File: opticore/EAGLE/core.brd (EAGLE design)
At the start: 100.3 x 82.6 mm, 121 parts, among them IC1 MCP1825S-3302E, IC2 MC33269T-5.0, J1 POWER_JACKSLT, Q1 MMDT3904, Q2 2N3904, Q3 2N3904, Q4 2N3904, Q5 2N3904, Q6 2N3904, Q7 2N3904, Q8 2N3904, U2 STM32F10XCXT6, U3 SST25VF040B-S2, U4 NL17SZ125SOT553, X1 USB-MICROB, X2 IPEX-20279-001E, Y1 32Khz, Y2 8Mhz

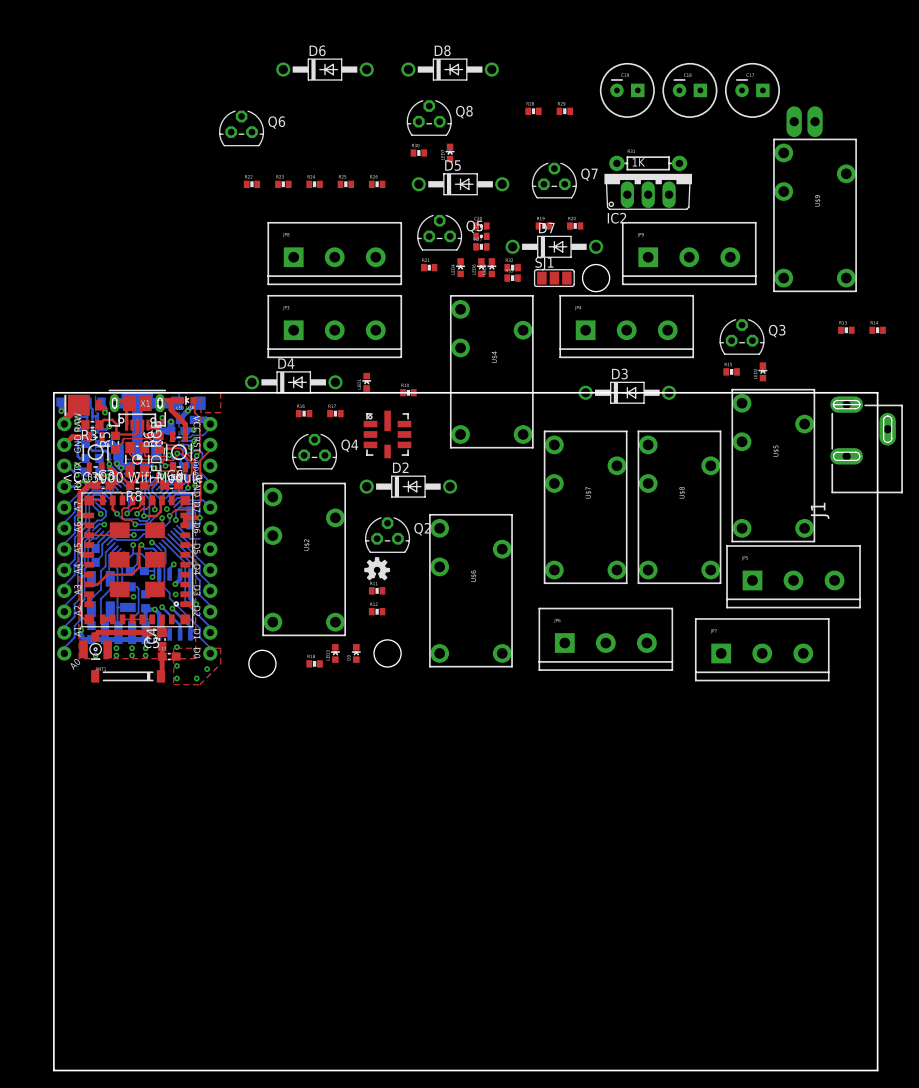
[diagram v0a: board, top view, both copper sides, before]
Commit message: Initial placement of relays
Still need to do a lot of work. Placement is temporary.

LEDs and the rest of the components need to be placed.

One problem is that I can't move what they originally did. Option #1: Redo what they did. (not happening) Option #2: Try adding their schematic as a part then placing it on a new shm. Option #3: Try to find a way to move it online.

Signed-off-by: Scott Lerner <scottphiliplerner@gmail.com>
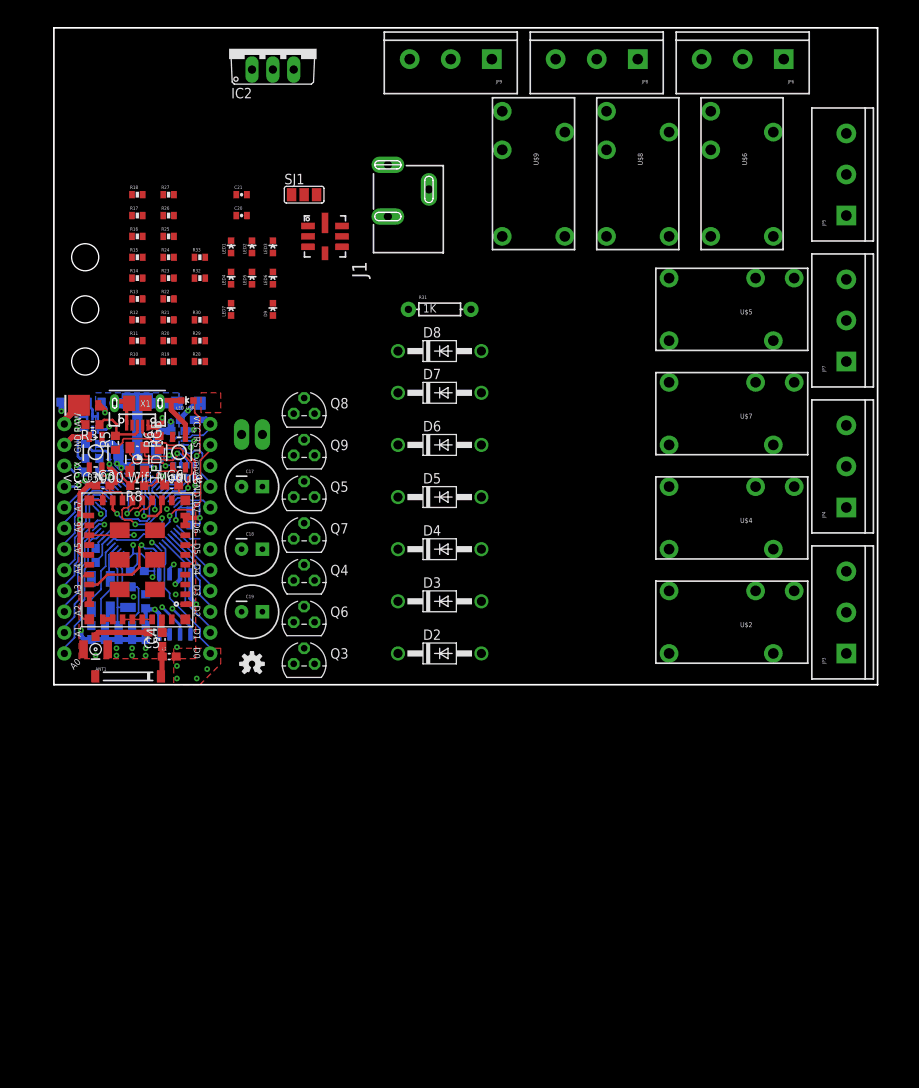
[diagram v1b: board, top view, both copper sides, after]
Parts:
- removed Q1: MMDT3904, SparkFun-DiscreteSemi:SOT363
- removed U$1: SPARK_LOGO2, Spark:SPARK_LOGO2
- added Q9: 2N3904, transistor-npn:TO92
- Q2: value 2N3904 -> MMDT3904; device transistor-npn:TO92 -> SparkFun-DiscreteSemi:SOT363
- moved R14 90.4 mm to (10.2, 49.5)
- moved R13 86.4 mm to (10.2, 47.0)
- moved C19 78.2 mm to (24.1, 8.89)
- moved JP3 78.0 mm to (96.5, 3.81), turned to 90 degrees
- moved C17 77.8 mm to (24.1, 24.1)
- moved JP10 77.3 mm to (22.9, 30.5)
- moved C18 77.3 mm to (24.1, 16.5)
- moved JP6 76.0 mm to (88.9, 76.2), turned to 180 degrees
- moved R15 73.7 mm to (10.2, 52.1)
- moved Q3 66.3 mm to (30.5, 2.54)
- moved LED2 64.1 mm to (24.1, 53.3)
- moved J1 63.1 mm to (38.1, 49.5)
- moved STANDOFF2 62.3 mm to (3.81, 52.1)
- moved R18 61.1 mm to (10.2, 59.7)
- moved U$6 60.6 mm to (83.8, 63.5)
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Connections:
- net +3V3: now also Q2.3; no longer Q1.3
- net GND: now also Q2.1, Q9.3; no longer Q1.1, Q2.3
- net N$13: now also Q2.5, Q2.6; no longer Q1.5, Q1.6
- net N$16: now also Q2.4; no longer Q1.4
- net N$18: now also Q3.1; no longer Q2.1
- net N$19: now also Q4.1; no longer Q3.1
- net N$20: now also Q4.2; no longer Q3.2
- net N$22: now also Q6.1; no longer Q4.1
- net N$23: now also Q6.2; no longer Q4.2
- net N$24: now also Q3.2; no longer Q2.2
- net N$26: now also Q7.1; no longer Q5.1
- net N$27: now also Q7.2; no longer Q5.2
- net N$29: now also Q5.1; no longer Q6.1
- net N$30: now also Q5.2; no longer Q6.2
- net N$32: now also Q8.1; no longer Q7.1
- net N$33: now also Q8.2; no longer Q7.2
- net N$35: now also Q9.1; no longer Q8.1
- net N$36: now also Q9.2; no longer Q8.2
- net N$8: now also Q2.2; no longer Q1.2
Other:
- board size 100.3 x 82.6 mm -> 100.3 x 80 mm

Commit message: Finished Initial Placement
I still need to route everything, but I think it's a pretty
space-efficient design as is. Probably needs to be organized a little
better.

NOTE: With the free version of EAGLE, I cannot make a board bigger than
100mm x 80mm. In those dimensions, I cannot place all relays in a
straight line. Hence the inverted 'L' shape.
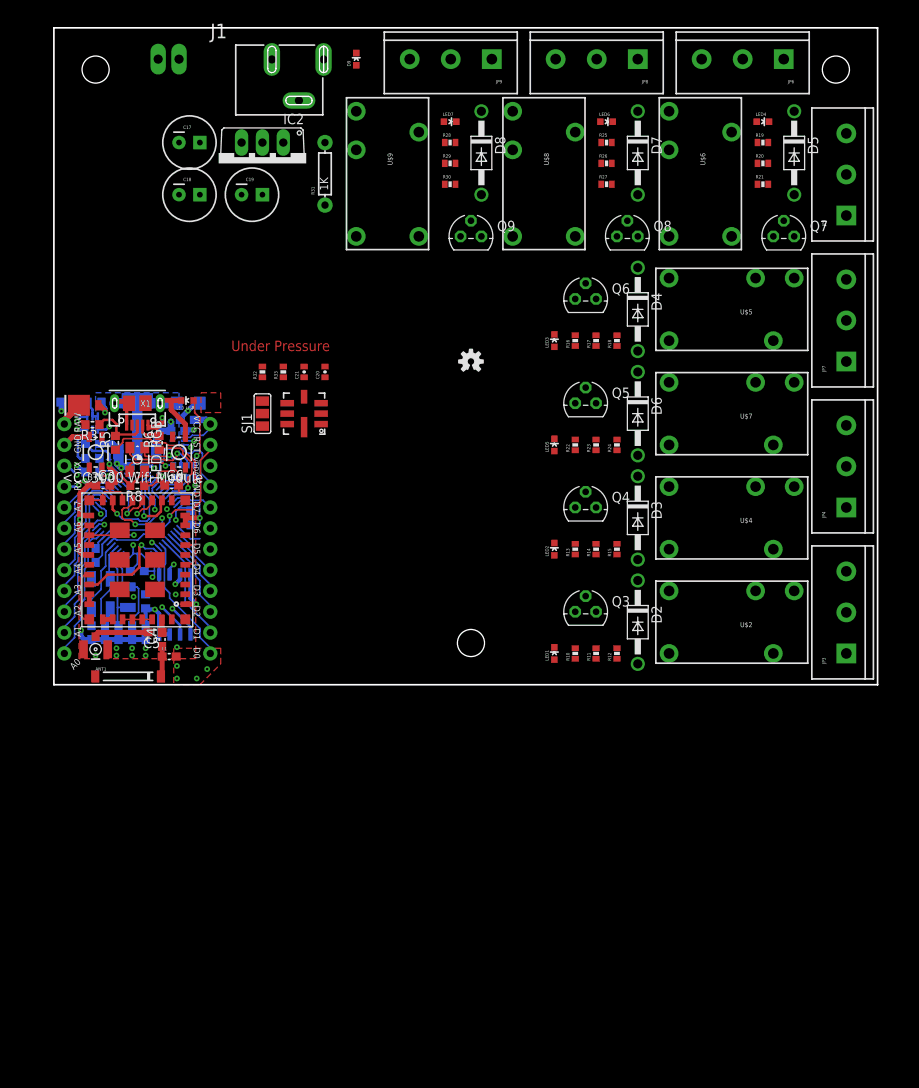
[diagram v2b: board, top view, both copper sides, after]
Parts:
- moved STANDOFF2 94.3 mm to (95.2, 74.9)
- moved R19 77.1 mm to (86.4, 66.0)
- moved R20 75.5 mm to (86.4, 63.5)
- moved R21 74.2 mm to (86.4, 61.0)
- moved R12 71.2 mm to (68.6, 3.81), turned to 90 degrees
- moved Q7 69.1 mm to (88.9, 54.6)
- moved R15 68.4 mm to (68.6, 16.5), turned to 90 degrees
- moved R11 67.6 mm to (66.0, 3.81), turned to 90 degrees
- moved LED4 67.5 mm to (86.4, 68.6), turned to 270 degrees
- moved R14 64.9 mm to (66.0, 16.5), turned to 90 degrees
- moved R10 64.1 mm to (63.5, 3.81), turned to 90 degrees
- moved LED1 63.3 mm to (61.0, 3.81)
- moved R13 61.4 mm to (63.5, 16.5), turned to 90 degrees
- moved R18 61.1 mm to (68.6, 41.9), turned to 90 degrees
- moved D5 60.2 mm to (90.2, 64.8), turned to 270 degrees
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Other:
- board text added: "Under Pressure"

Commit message: Close to final revision
I'm working on laying down the final placement as well as the ground
planes. I'll try and work on it soon.
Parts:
- removed ANT1: AT8010, Spark:AT8010
- removed BTN, RESET: KMR211GLFS, Spark:TACTILE_SWITCH_SMD
- removed C1, C2: 4.7uF, rcl:C0603
- removed C10, C11: 22pF, rcl:C0603
- removed C12, C13, C14, C16, C3, C6, C7: 100nF, rcl:C0603
- removed C15: 10uF, Spark:EIA3216
- removed C4: 2.2pF, rcl:C0603
- removed C5, C8, C9: 10pF, rcl:C0603
- removed D8: 1N4004, diode:DO41-10
- removed D9: GREEN, SparkFun-LED:LED-0603
- removed IC1: MCP1825S-3302E, Spark:SOT223
- removed JP1, JP2: M12PTH, Spark:1X12-SMALL-PADS
- removed JP3, JP4, JP5, JP6, JP7, JP8, JP9: (no value), SparkFun-Connectors:SCREWTERMINAL-5MM-3
- removed L1: 2.2nH, SparkFun-Passives:0603
- removed L2: Bead, SparkFun-Passives:0603
- removed LED_RGB: (no value), Spark:P-LCC-4-3
- removed LED_USR: (no value), SparkFun:LED-0603
- removed LOGO1: OSHW-LOGOS, SparkFun-Aesthetics:OSHW-LOGO-S
- removed Q8, Q9: 2N3904, transistor-npn:TO92
- removed R25, R27, R28, R30: 1K, SparkFun-Passives:0402-RES
- removed R26, R29: 10K, SparkFun-Passives:0402-RES
- removed R31: 1K, SparkFun-Passives:AXIAL-0.3
- removed R32, R33: 4.7K, SparkFun-Passives:0402-RES
- removed RN1: EXB-38V102JV, resistor-dil:EXB38V
- removed STANDOFF1, STANDOFF2, STANDOFF3: STAND-OFF, SparkFun-Electromechanical:STAND-OFF
- removed U1: (no value), CC3000:CC3000
- removed U2: STM32F10XCXT6, stm32:TQFP48
- removed U3: SST25VF040B-S2, Spark:SOIC127P790X216-8N
- removed U4: NL17SZ125SOT553, Spark:SOT-553
- removed X2: IPEX-20279-001E, Spark:IPEX-20279-001E
- removed Y1: 32Khz, Spark:FC135
- removed Y2: 8Mhz, SparkFun-FreqCtrl:CRYSTAL-SMD-5X3
- added JP11, JP12: M12PTH, Spark:1X12-SMALL-PADS
- added LED8: (no value), SparkFun-LED:LED3MM
- added LOGO2: OSHW-LOGOL, SparkFun-Aesthetics:OSHW-LOGO-L
- added Q1: 2N3904, transistor-npn:TO92
- C17, C18, C19: value (none) -> 100uF
- D1: value DIODE -> 1N4004; device Spark:DIODE-DO-220AA(SMP) -> diode:DO41-10
- LED1, LED2, LED3, LED4, LED5, LED6, LED7: value RED -> (none); device SparkFun-LED:LED-0603 -> SparkFun-LED:LED3MM
- Q2: value MMDT3904 -> 2N3904; device SparkFun-DiscreteSemi:SOT363 -> transistor-npn:TO92
- R1, R8: value 10K -> 1K; device rcl:R0603 -> SparkFun-Resistors:AXIAL-0.3
- R10, R13, R16, R19, R24: device SparkFun-Passives:0402-RES -> SparkFun-Resistors:AXIAL-0.3
- R11, R14, R17, R20: value 10K -> 1K; device SparkFun-Passives:0402-RES -> SparkFun-Resistors:AXIAL-0.3
- R12, R15, R18, R21: value 1K -> 10K; device SparkFun-Passives:0402-RES -> SparkFun-Resistors:AXIAL-0.3
- R2: value 33K -> 1K; device rcl:R0603 -> SparkFun-Resistors:AXIAL-0.3
- R22: value 1K -> 4.7K; device SparkFun-Passives:0402-RES -> SparkFun-Resistors:AXIAL-0.3
- R23: value 10K -> 4.7K; device SparkFun-Passives:0402-RES -> SparkFun-Resistors:AXIAL-0.3
- R3: value 1K5 -> 10K; device rcl:R0603 -> SparkFun-Resistors:AXIAL-0.3
- R4: device rcl:R0603 -> SparkFun-Resistors:AXIAL-0.3
- R5: value 22 -> 1K; device rcl:R0603 -> SparkFun-Resistors:AXIAL-0.3
- R6: value 22 -> 10K; device rcl:R0603 -> SparkFun-Resistors:AXIAL-0.3
- R7: value 47K -> 1K; device rcl:R0603 -> SparkFun-Resistors:AXIAL-0.3
- R9: value 1K -> 10K; device rcl:R0603 -> SparkFun-Resistors:AXIAL-0.3
- X1: value USB-MICROB -> FFKV8; device Spark:USB-MICROB-SLOT-HOLE -> con-phoenix-508:FFKV8
- moved JP10 106.0 mm to (88.9, 2.54), turned to 180 degrees
- moved J1 99.0 mm to (73.7, -3.81), turned to 0 degrees
- moved C17 89.5 mm to (86.4, 10.2), turned to 270 degrees
- moved SJ1 72.7 mm to (91.4, 63.5), turned to 0 degrees
- moved C19 72.2 mm to (69.8, 3.81), turned to 270 degrees
- moved C18 70.9 mm to (67.3, 10.2), turned to 270 degrees
- moved IC2 70.6 mm to (61.0, 2.54)
- moved U$2 67.5 mm to (17.8, 21.6), turned to 180 degrees
- moved C20 65.1 mm to (94.0, 61.0)
- moved U$3 65.1 mm to (91.4, 55.9)
- moved C21 62.7 mm to (88.9, 61.0)
- moved LED1 58.4 mm to (20.3, 45.7), turned to 90 degrees
- moved U$8 54.2 mm to (94.0, 21.6), turned to 180 degrees
- moved LED7 53.4 mm to (96.5, 45.7), turned to 90 degrees
- moved U$4 53.4 mm to (30.5, 21.6), turned to 180 degrees
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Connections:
- removed net BTN: BTN.3, U2.20
- removed net LED1: LED_USR.A, RN1.4
- removed net LED2: RN1.8, U2.29
- removed net LED3: RN1.7, U2.30
- removed net LED4: RN1.6, U2.31
- removed net MAIN1: JP3.2, U$2.4
- removed net MAIN2: JP4.2, U$4.4
- removed net MAIN3: JP7.2, U$7.4
- removed net MAIN4: JP5.2, U$5.4
- removed net MAIN5: JP6.2, U$6.4
- removed net MAIN6: JP8.2, U$8.4
- removed net MAIN7: JP9.2, U$9.4
- removed net MEM_CS: R9.1, U2.46, U3.1
- removed net N$10: LED_RGB.1, RN1.1
- removed net N$12: LED_RGB.3, RN1.2
- removed net N$13: Q2.5, Q2.6, R1.1, R2.2
- removed net N$14: LED_RGB.4, RN1.3
- removed net N$15: U1.SDA_CC3000, U1.SDA_EEPROM
- removed net N$16: Q2.4, R3.2
- removed net N$17: LED2.A, R13.1
- removed net N$21: LED3.A, R16.1
- removed net N$25: LED4.A, R19.1
- removed net N$28: LED5.A, R22.1
- removed net N$31: LED6.A, R25.1
- removed net N$34: LED7.A, R28.1
- removed net N$43: R32.2, SJ1.3
- removed net N$44: R33.2, SJ1.1
- removed net NC1: JP3.3, U$2.2
- removed net NC2: JP4.3, U$4.2
- removed net NC3: JP7.3, U$7.2
- removed net NC4: JP5.3, U$5.2
- removed net NC5: JP6.3, U$6.2
- removed net NC6: JP8.3, U$8.2
- removed net NC7: JP9.3, U$9.2
- removed net OSC32_IN: C9.1, U2.3, Y1.X1
- removed net OSC32_OUT: C8.1, U2.4, Y1.X2
- removed net OSC_IN: C11.1, U2.5, Y2.1
- removed net OSC_OUT: C10.1, U2.6, Y2.3
- removed net SPI_DOUT: U1.SPI_DOUT, U4.IN
- removed net SPI_MISO: U2.27, U3.2, U4.OUT
- removed net SPI_MOSI: U1.SPI_DIN, U2.28, U3.5
- removed net SPI_SCK: U1.SPI_CLK, U2.26, U3.6
- removed net USBM: R6.1, U2.32
- removed net USBP: R5.1, U2.33
- removed net USB_DISC: R4.1, R7.2, U2.21
- removed net UVCC: D1.ANODE, R1.2, X1.VBUS
- removed net WIFI_CS: U1.SPI_CS, U2.25, U4./OE
- removed net WIFI_EN: U1.VBAT_SW_EN, U2.45
- removed net WIFI_INT: U1.SPI_IRQ, U2.22
- new net MAIN: U$2.4, U$4.4, U$5.4, U$6.4, U$7.4, U$8.4, U$9.4, X1.8A
- net !RST: now also JP12.2; no longer C6.2, JP2.2, R8.1, RESET.1, U2.7
- net +3V3: now also JP12.1; no longer C12.1, C14.1, C16.1, C2.1, C3.1, C7.1, IC1.3, JP2.1, L2.1, LED_RGB.2, Q2.3, R7.1, R8.2, R9.2, U1.VBAT_IN, U1.VIO_HOST, U2.1, U2.24, U2.36, U2.48, U3.3, U3.7, U3.8, U4.VCC
- net 5V: now also D1.C, R1.P$2, R10.P$2, R13.P$2, R16.P$2, R19.P$2, R24.P$1, R4.P$2, R7.P$2; no longer D8.C, R10.2, R13.2, R16.2, R19.2, R22.2, R25.2, R28.2, R31.P$1
- net A2: now also JP11.10; no longer JP1.10, U2.14
- net A3: now also JP11.9; no longer JP1.9, U2.15
- net A4: now also JP11.8; no longer JP1.8, U2.16
- net A5: now also JP11.7; no longer JP1.7, U2.17
- net A6: now also JP11.6; no longer JP1.6, U2.18
- net A7: now also JP11.5; no longer JP1.5, U2.19
- net D7: now also JP12.5; no longer JP2.5, RN1.5, U2.34
- net GND: now also JP11.2, JP12.4, LED8.K, Q1.3, Q2.3, R12.P$1, R15.P$1, R18.P$1, R21.P$1, R3.P$1, R6.P$1, R9.P$1; no longer BTN.2, C1.2, C10.2, C11.2, C12.2, C13.2, C14.2, C15.C, C16.2, C2.2, C3.2, C6.1, C7.2, C8.2, C9.2, D9.C, IC1.2, IC1.4, JP1.2, JP2.4, L1.2, LED_USR.C, Q2.1, Q8.3, Q9.3, R11.1, R14.1, R17.1, R2.1, R20.1, R23.1, R26.1, R29.1, RESET.4, U1.EXT_32K, U1.GND@1, U1.GND@10, U1.GND@11, U1.GND@16, U1.GND@18, U1.GND@20, U1.GND@22, U1.GND@25, U1.GND@31, U1.GND@32, U1.GND@33, U1.GND@34, U1.GND@36, U1.GND@37, U1.GND@38, U1.GND@39, U1.GND@40, U1.GND@41, U1.GND@42, U1.GND@43, U1.GND@44, U1.GND@45, U1.GND@46, U1.GND@9, U2.23, U2.35, U2.44, U2.47, U2.8, U3.4, U4.GND, X1.GND, X1.MT1, X1.MT2, X2.2@1, X2.2@2
- net N$1: now also LED1.A, R1.P$1; no longer R3.1, R5.2, X1.D+
- net N$18: now also D1.A, LED1.K, Q1.1; no longer D2.A, LED1.C, Q3.1
- net N$19: now also D2.A, LED2.K, Q2.1; no longer D3.A, LED2.C, Q4.1
- net N$2: now also LED2.A, R4.P$1; no longer C5.2, X2.1
- net N$20: now also Q2.2, R5.P$2, R6.P$2; no longer Q4.2, R14.2, R15.1
- net N$22: now also D5.A, LED5.K, Q5.1; no longer D4.A, LED3.C, Q6.1
- net N$23: now also Q5.2, R14.P$2, R15.P$2; no longer Q6.2, R17.2, R18.1
- net N$24: now also Q1.2, R2.P$2, R3.P$2; no longer Q3.2, R11.2, R12.1
- net N$26: now also D6.A, LED6.K, Q6.1; no longer D5.A, LED4.C, Q7.1
- net N$27: now also Q6.2, R17.P$2, R18.P$2; no longer Q7.2, R20.2, R21.1
- net N$29: now also D3.A, LED3.K, Q3.1; no longer D6.A, LED5.C, Q5.1
- net N$3: now also LED5.A, R13.P$1; no longer ANT1.SIG, C4.1, L1.1
- net N$30: now also Q3.2, R8.P$2, R9.P$2; no longer Q5.2, R23.2, R24.1
- net N$32: now also LED7.K, Q7.1; no longer LED6.C, Q8.1
- net N$33: now also Q7.2, R20.P$2, R21.P$2; no longer Q8.2, R26.2, R27.1
- net N$35: now also D4.A, LED4.K, Q4.1; no longer D8.A, LED7.C, Q9.1
- net N$36: now also Q4.2, R11.P$2, R12.P$2; no longer Q9.2, R29.2, R30.1
- net N$39: now also LED8.A, R24.P$2; no longer D9.A, R31.P$2
- net N$4: now also LED6.A, R16.P$1; no longer LED1.A, R10.1
- net N$5: now also LED3.A, R7.P$1; no longer C4.2, C5.1, U1.RF_ANT
- net N$6: now also LED4.A, R10.P$1; no longer R6.2, X1.D-
- net N$7: now also LED7.A, R19.P$1; no longer U1.SCL_CC3000, U1.SCL_EEPROM
- net N$8: now also R22.P$2, SJ1.3; no longer Q2.2, R4.2
- net N$9: now also R23.P$2, SJ1.1; no longer U1.WL_EN1, U1.WL_EN2
- net NO1: now also X1.7A; no longer JP3.1
- net NO2: now also X1.6A; no longer JP4.1
- net NO3: now also X1.5A; no longer JP7.1
- net NO4: now also U$9.3, X1.4A; no longer JP5.1, U$5.3
- net NO5: now also U$5.3, X1.3A; no longer JP6.1, U$6.3
- net NO6: now also U$6.3, X1.2A; no longer JP8.1, U$8.3
- net NO7: now also U$8.3, X1.1A; no longer JP9.1, U$9.3
- net RAW: now also JP11.1; no longer C1.1, D1.CATHODE, IC1.1, JP1.1
- net RELAY1: now also JP12.12, R2.P$1; no longer JP2.12, R12.2, U2.43
- net RELAY2: now also JP12.11, R5.P$1; no longer JP2.11, R15.2, U2.42
- net RELAY3: now also JP12.10, R8.P$1; no longer JP2.10, R24.2, U2.41
- net RELAY4: now also JP12.9, R11.P$1; no longer JP2.9, R18.2, U2.40
- net RELAY5: now also JP12.8, R14.P$1; no longer JP2.8, R21.2, U2.39
- net RELAY6: now also JP12.7, R17.P$1; no longer JP2.7, R27.2, U2.38
- net RELAY7: now also JP12.6, R20.P$1; no longer JP2.6, R30.2, U2.37
- net RX: now also JP11.4; no longer JP1.4, U2.13
- net SCL: now also JP11.11, R23.P$1; no longer JP1.11, R33.1, U2.11
- net SDA: now also JP11.12, R22.P$1; no longer JP1.12, R32.1, U2.10
- net TX: now also JP11.3; no longer JP1.3, U2.12
- net VDDA: now also JP12.3; no longer C13.1, C15.A, JP2.3, L2.2, U2.9
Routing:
- net GND: track 115.6 -> 0.00 mm, vias 27 -> 0
- net +3V3: track 60.6 -> 0.00 mm, vias 10 -> 0
- net !RST: track 32.5 -> 0.00 mm, vias 1 -> 0
- net VDDA: track 31.0 -> 0.00 mm, vias 2 -> 0
- net SPI_MOSI: track 29.5 -> 0.00 mm, vias 2 -> 0
- net SPI_SCK: track 29.5 -> 0.00 mm, vias 2 -> 0
- net WIFI_CS: track 25.9 -> 0.00 mm, vias 2 -> 0
- net RAW: track 24.7 -> 0.00 mm, vias 1 -> 0
- net USBP: track 18.9 -> 0.00 mm, vias 1 -> 0
- net SPI_MISO: track 18.3 -> 0.00 mm, vias 2 -> 0
- net SDA: track 16.0 -> 0.00 mm
- net A2: track 15.9 -> 0.00 mm
- net SPI_DOUT: track 15.0 -> 0.00 mm, vias 2 -> 0
- net RELAY1: track 15.0 -> 0.00 mm
- net A3: track 13.6 -> 0.00 mm
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- removed copper zone on layer 15, net +3V3
- removed copper zone on layer 1, net GND
- removed copper zone on layer 16, net GND
- removed copper zone on layer 2, net GND
- removed copper zone on layer 1, net N$11
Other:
- board text removed: "A0"
- board text removed: "A1"
- board text removed: "A2"
- board text removed: "A3"
- board text removed: "A4"
- board text removed: "A5"
- board text removed: "A6"
- board text removed: "A7"
- board text removed: "BTN"
- board text removed: "D0"
- board text removed: "D1"
- board text removed: "D2"
- board text removed: "D3"
- board text removed: "D4"
- board text removed: "D5"
- board text removed: "D6"
- board text removed: "D7"
- board text removed: "GND"
- board text removed: "RAW"
- board text removed: "RST"
- board text removed: "RX"
- board text removed: "TX"
- board text removed: "VCC"
- board text removed: "VDDA"

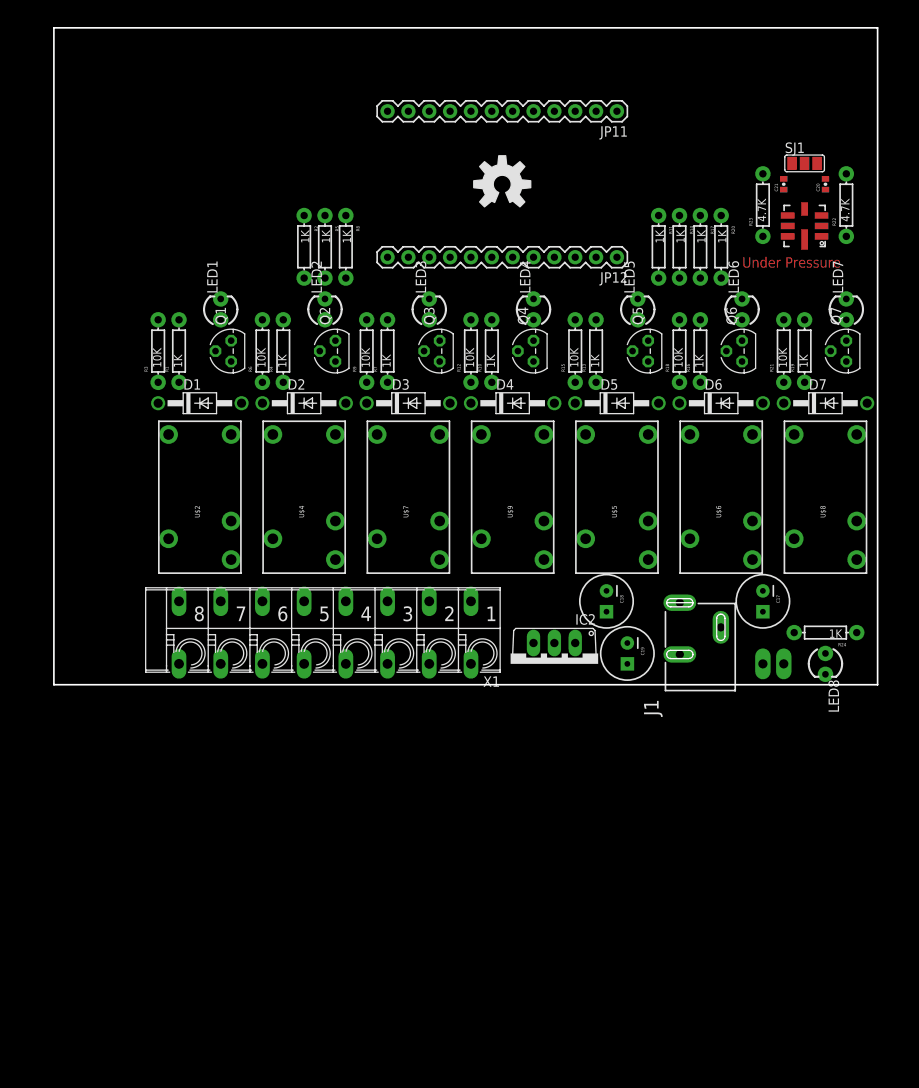
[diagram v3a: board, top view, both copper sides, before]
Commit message: Partially done with routing
Mainly working on layout now. Adding a custom image to see how it looks.
Also, I think I'm going to replace the capacitors for the pressure
sensor.
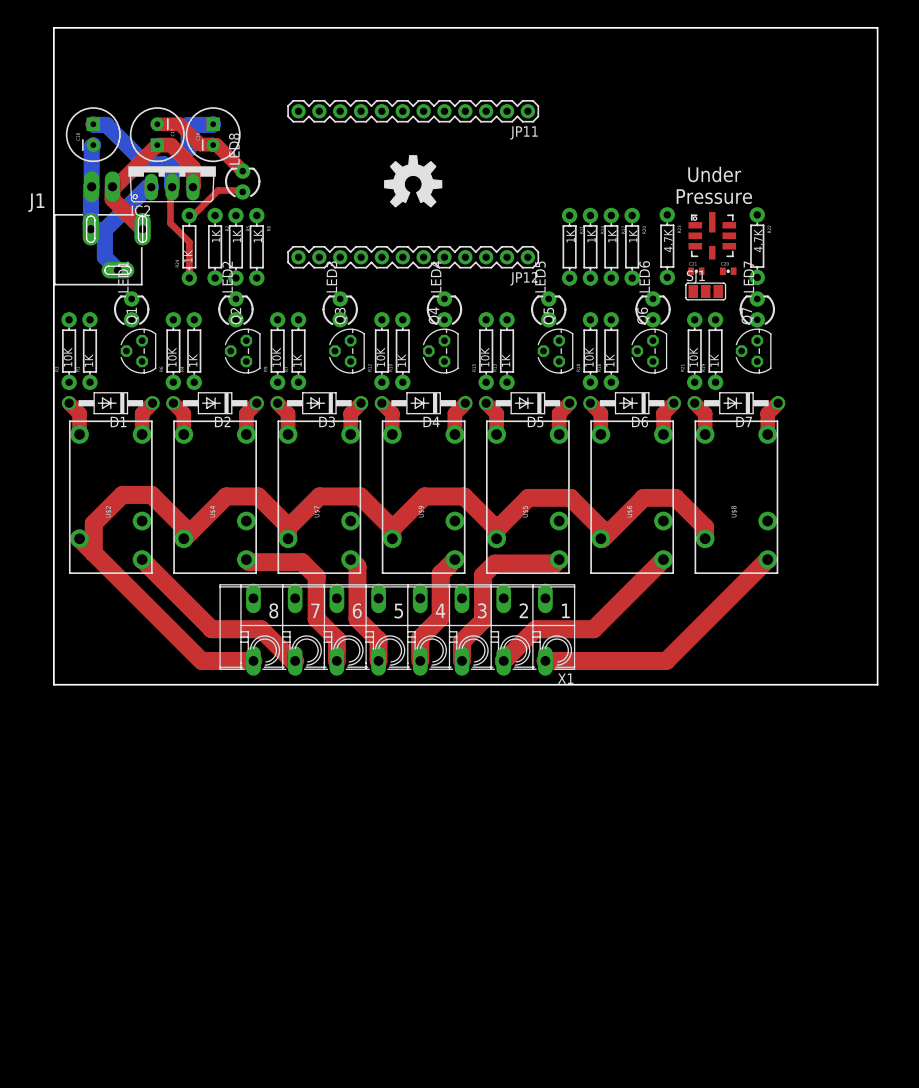
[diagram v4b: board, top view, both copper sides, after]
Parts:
- moved JP10 102.4 mm to (4.60, 60.7), turned to 0 degrees
- moved J1 98.5 mm to (-3.00, 58.1), turned to 270 degrees
- moved C17 93.1 mm to (12.6, 67.0)
- moved LED8 92.1 mm to (23.0, 61.3), turned to 90 degrees
- moved R24 90.6 mm to (16.5, 53.3), turned to 90 degrees
- moved C18 84.5 mm to (4.80, 67.0), turned to 90 degrees
- moved C19 80.9 mm to (19.4, 67.0), turned to 90 degrees
- moved IC2 76.4 mm to (14.4, 63.1), turned to 0 degrees
- moved SJ1 19.7 mm to (79.4, 47.9)
- moved C20 15.9 mm to (82.1, 50.4), turned to 0 degrees
- moved C21 15.0 mm to (78.3, 50.4), turned to 0 degrees
- moved R23 12.7 mm to (74.7, 53.4), turned to 270 degrees
- moved R22 11.9 mm to (85.7, 53.4), turned to 270 degrees
- moved U$3 11.3 mm to (80.2, 54.7), turned to 0 degrees
- moved R21 10.8 mm to (78.1, 40.6)
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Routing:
- net MAIN: track 0.00 -> 133.2 mm
- net 5V: track 0.00 -> 65.9 mm
- net GND: track 0.00 -> 38.3 mm
- net NO7: track 0.00 -> 32.2 mm
- net NO6: track 0.00 -> 24.6 mm
- net NO1: track 0.00 -> 23.8 mm
- net N$37: track 0.00 -> 22.2 mm
- net NO5: track 0.00 -> 21.6 mm
- net NO2: track 0.00 -> 20.7 mm
- net NO4: track 0.00 -> 14.1 mm
- net NO3: track 0.00 -> 13.8 mm
- net N$39: track 0.00 -> 7.84 mm
- net N$32: track 0.00 -> 4.34 mm
- net N$35: track 0.00 -> 4.34 mm
- net N$29: track 0.00 -> 4.34 mm
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
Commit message: Under Pressure
Adding a bit of personality to the board. Essentially have a good
layout. Still need to do the changes from 2 commits ago.
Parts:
- moved C20 14.4 mm to (69.1, 56.5)
- moved C21 14.4 mm to (65.3, 56.5)
- moved U$3 14.4 mm to (67.2, 60.8)
- moved R23 14.3 mm to (61.7, 59.4)
- moved R22 14.3 mm to (72.7, 59.3)
- moved SJ1 13.6 mm to (67.2, 54.0)
- moved R11 13.2 mm to (76.0, 53.8)
- moved R14 13.2 mm to (78.5, 53.8)
- moved R17 13.2 mm to (81.0, 53.8)
- moved R20 13.2 mm to (83.6, 53.8)
- moved LOGO2 7.61 mm to (36.2, 61.4)
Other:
- board size 100.3 x 80 mm -> 90.1 x 72.3 mm
- board text added: "D:/Users/Scott/Documents/GitHub/optisprk/eagle_custom_icon.bmp"
